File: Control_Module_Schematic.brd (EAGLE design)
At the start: 67 x 47 mm, 30 parts, among them U2 ATMEGA328P_TQFP

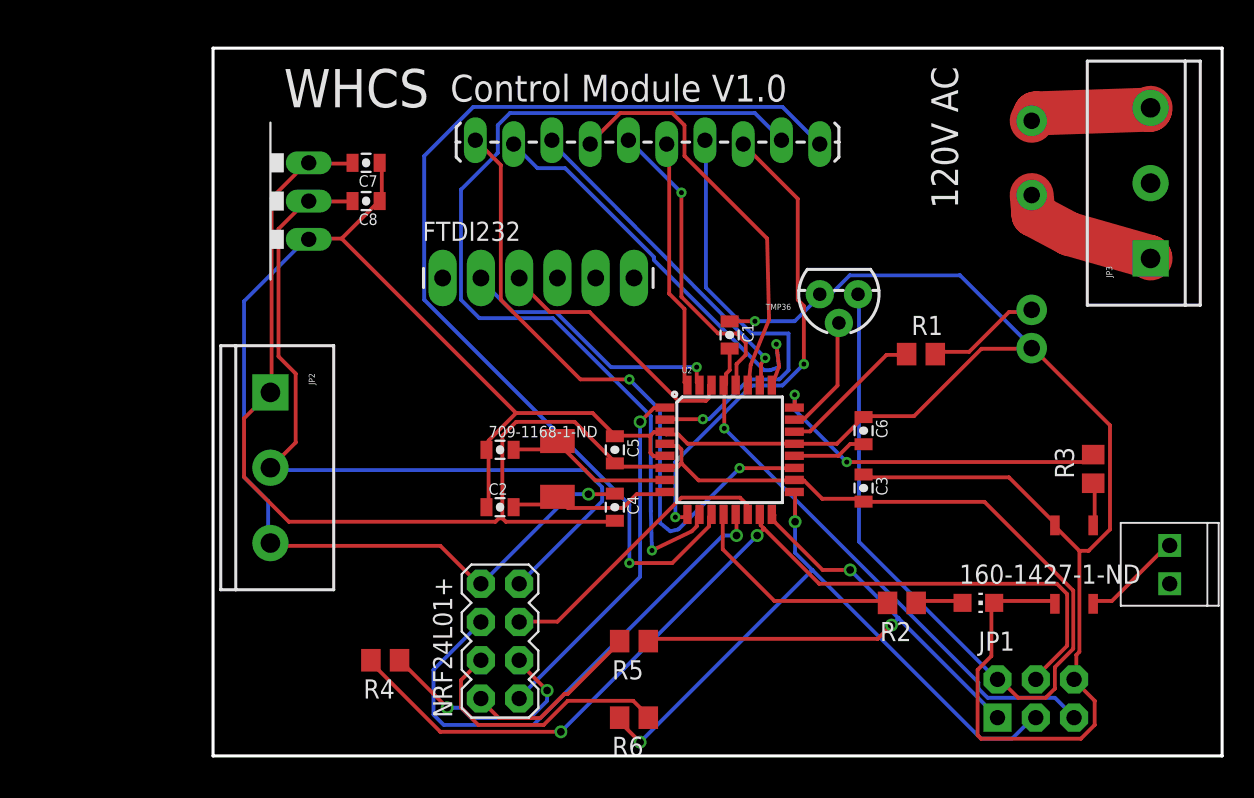
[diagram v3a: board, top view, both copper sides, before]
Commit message: Enhanced crystal footprint
Also did some changing of the route placements to make them have better
spacing.

Added documentation to the TPlace layer to show how the power should be
connected.
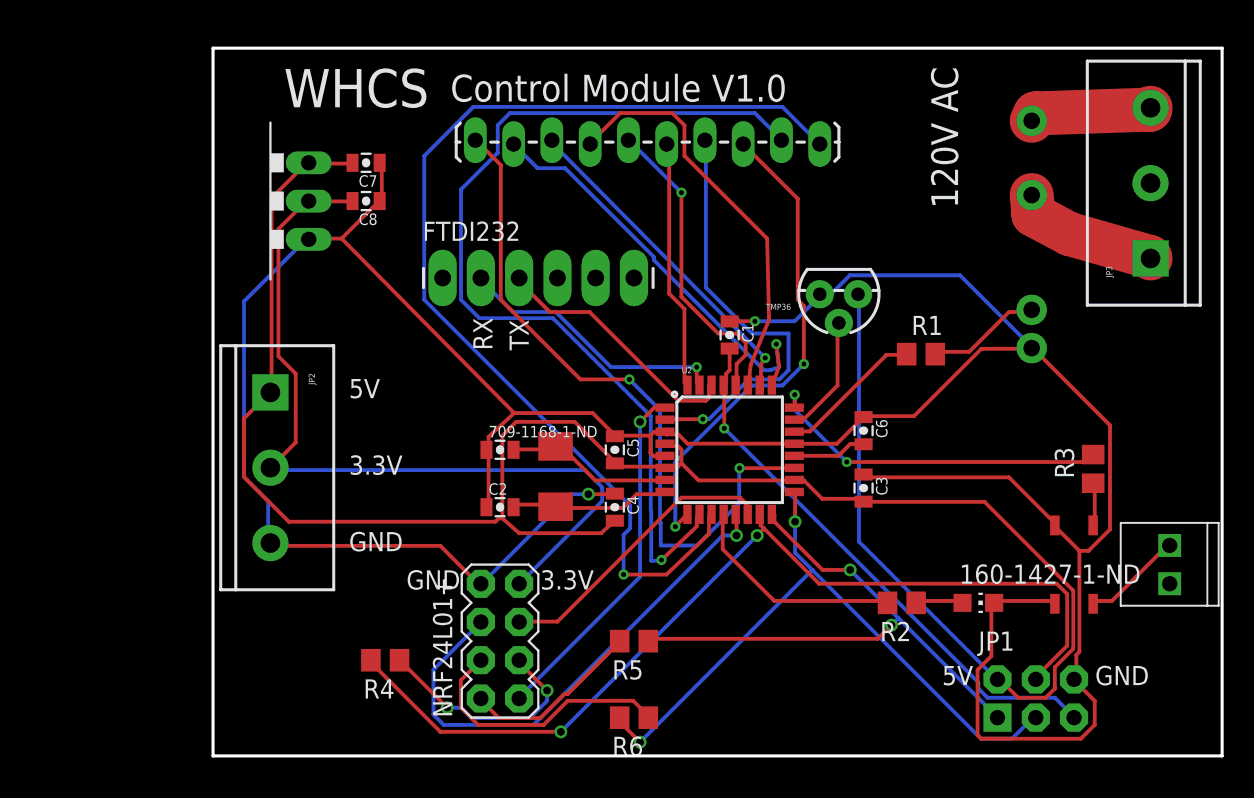
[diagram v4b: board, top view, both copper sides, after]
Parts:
- moved CRYS 0.52 mm to (22.7, 18.5)
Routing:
- net ADC6: track 43.2 -> 46.3 mm
- net PD7: track 68.4 -> 70.4 mm
- net PD6: track 61.5 -> 62.8 mm
- net PD5: track 32.0 -> 32.9 mm
- net 5V: track 143.7 -> 144.3 mm
- net N$15: track 11.1 -> 11.7 mm
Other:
- board text added: "3.3V"
- board text added: "5V"
- board text added: "GND"
- board text added: "RX"
- board text added: "TX"
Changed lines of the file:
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@@
 <text x="15.748" y="43.434" size="1.778" layer="21">Control Module V1.0</text>
 <text x="49.4538" y="36.3347" size="1.778" layer="21" rot="R90">120V AC</text>
+<text x="12.827" y="11.049" size="1.27" layer="21">GND</text>
+<text x="21.717" y="11.049" size="1.27" layer="21">3.3V</text>
+<text x="58.547" y="4.699" size="1.27" layer="21">GND</text>
+<text x="48.387" y="4.699" size="1.27" layer="21">5V</text>
+<text x="17.272" y="29.083" size="1.27" layer="21" rot="R270">RX</text>
+<text x="19.685" y="28.956" size="1.27" layer="21" rot="R270">TX</text>
+<text x="9.017" y="23.749" size="1.27" layer="21">5V</text>
+<text x="9.017" y="13.589" size="1.27" layer="21">GND</text>
+<text x="9.017" y="18.669" size="1.27" layer="21">3.3V</text>
 </plain>
 <attributes>
@@
 <element name="C5" library="SparkFun-Capacitors" package="0805-CAP" value="100nF" x="26.67" y="20.32" rot="R270"/>
 <element name="CPC1002NTR" library="WHCS" package="CPC1002N" value="CPC1002NTR" x="57.15" y="12.7"/>
-<element name="CRYS" library="WHCS" package="CRYS-5X3.2" value="NDK-NX5032GA" x="22.86" y="19.05" rot="R270"/>
+<element name="CRYS" library="WHCS" package="CRYS-5X3.2" value="NDK-NX5032GA" x="22.733" y="18.542" rot="R270"/>
 <element name="FTDI232" library="SparkFun-Connectors" package="1X06_LONGPADS" value="" x="15.24" y="31.7246"/>
 <element name="JP1" library="SparkFun-Connectors" package="2X3-NS" value="AVR_SPI" x="54.61" y="3.81" smashed="yes">
@@
 <wire x1="6.1722" y1="39.3192" x2="6.35" y2="39.37" width="0.254" layer="1"/>
 <wire x1="3.8862" y1="24.2316" x2="3.81" y2="24.13" width="0.254" layer="1"/>
-<wire x1="19.431" y1="15.5448" x2="26.5176" y2="15.5448" width="0.254" layer="1"/>
-<wire x1="19.2024" y1="15.7734" x2="19.431" y2="15.5448" width="0.254" layer="1"/>
+<wire x1="20.32" y1="14.7828" x2="25.7556" y2="14.7828" width="0.254" layer="1"/>
+<wire x1="19.2024" y1="15.7734" x2="20.32" y2="14.7828" width="0.254" layer="1"/>
 <wire x1="19.2024" y1="21.2598" x2="19.2024" y2="15.7734" width="0.254" layer="1"/>
 <wire x1="20.1168" y1="22.1742" x2="19.2024" y2="21.2598" width="0.254" layer="1"/>
 <wire x1="24.003" y1="22.1742" x2="20.1168" y2="22.1742" width="0.254" layer="1"/>
 <wire x1="26.7462" y1="19.431" x2="24.003" y2="22.1742" width="0.254" layer="1"/>
-<wire x1="26.5176" y1="15.5448" x2="26.67" y2="15.61" width="0.254" layer="1"/>
+<wire x1="25.7556" y1="14.7828" x2="26.67" y2="15.61" width="0.254" layer="1"/>
 <wire x1="26.7462" y1="19.431" x2="26.67" y2="19.42" width="0.254" layer="1"/>
 <wire x1="26.7462" y1="19.2024" x2="29.9466" y2="19.2024" width="0.254" layer="1"/>
@@
 <wire x1="10.9728" y1="36.7792" x2="11.06" y2="36.83" width="0.254" layer="1"/>
 <wire x1="6.5024" y1="34.3408" x2="6.35" y2="34.29" width="0.254" layer="1"/>
-<wire x1="18.288" y1="20.9296" x2="18.288" y2="20.32" width="0.254" layer="1"/>
-<wire x1="20.1168" y1="22.7584" x2="18.288" y2="20.9296" width="0.254" layer="1"/>
-<wire x1="25.1968" y1="22.7584" x2="20.1168" y2="22.7584" width="0.254" layer="1"/>
+<wire x1="18.288" y1="21.1836" x2="18.288" y2="20.32" width="0.254" layer="1"/>
+<wire x1="19.9898" y1="22.7584" x2="18.288" y2="21.1836" width="0.254" layer="1"/>
+<wire x1="25.1968" y1="22.7584" x2="19.9898" y2="22.7584" width="0.254" layer="1"/>
 <wire x1="26.6192" y1="21.336" x2="25.1968" y2="22.7584" width="0.254" layer="1"/>
 <wire x1="18.288" y1="20.32" x2="18.15" y2="20.32" width="0.254" layer="1"/>
 <wire x1="26.6192" y1="21.336" x2="26.67" y2="21.22" width="0.254" layer="1"/>
-<wire x1="20.1168" y1="22.7584" x2="8.5344" y2="34.3408" width="0.254" layer="1"/>
+<wire x1="19.9898" y1="22.7584" x2="8.5344" y2="34.3408" width="0.254" layer="1"/>
 <wire x1="31.496" y1="20.7264" x2="38.4048" y2="20.7264" width="0.254" layer="1"/>
 <wire x1="30.8864" y1="21.336" x2="31.496" y2="20.7264" width="0.254" layer="1"/>
@@
 <wire x1="22.86" y1="20.8026" x2="25.3746" y2="18.288" width="0.254" layer="1"/>
 <wire x1="29.9466" y1="18.288" x2="29.9974" y2="18.32" width="0.254" layer="1"/>
-<wire x1="22.86" y1="20.8026" x2="22.86" y2="20.9" width="0.254" layer="1"/>
+<wire x1="22.86" y1="20.8026" x2="22.733" y2="20.542" width="0.254" layer="1"/>
 </signal>
 <signal name="N$15">
@@
 <wire x1="22.86" y1="17.145" x2="23.5458" y2="16.4592" width="0.254" layer="1"/>
 <wire x1="29.9466" y1="17.3736" x2="29.9974" y2="17.52" width="0.254" layer="1"/>
-<wire x1="22.86" y1="17.145" x2="22.86" y2="17.2" width="0.254" layer="1"/>
+<wire x1="22.86" y1="17.145" x2="22.733" y2="16.542" width="0.254" layer="1"/>
 </signal>
 <signal name="N$16">
@@
 <contactref element="JP4" pad="8"/>
 <contactref element="U2" pad="9"/>
-<wire x1="30.6832" y1="15.8496" x2="31.2928" y2="15.8496" width="0.254" layer="1"/>
-<wire x1="30.6832" y1="19.5072" x2="30.6832" y2="15.8496" width="0.254" layer="16"/>
+<wire x1="30.6832" y1="15.2146" x2="31.2928" y2="15.8496" width="0.254" layer="1"/>
+<wire x1="30.6832" y1="19.5072" x2="30.6832" y2="15.2146" width="0.254" layer="16"/>
 <wire x1="35.7632" y1="24.5872" x2="30.6832" y2="19.5072" width="0.254" layer="16"/>
 <wire x1="37.7952" y1="24.5872" x2="35.7632" y2="24.5872" width="0.254" layer="16"/>
@@
 <wire x1="31.2928" y1="15.8496" x2="31.49" y2="16.0274" width="0.254" layer="1"/>
 <wire x1="35.3568" y1="40.4368" x2="35.1917" y2="40.6146" width="0.254" layer="1"/>
-<via x="30.6832" y="15.8496" extent="1-16" drill="0.3302"/>
+<via x="30.6832" y="15.2146" extent="1-16" drill="0.3302"/>
 <via x="39.2176" y="26.0096" extent="1-16" drill="0.3302"/>
 </signal>
@@
 <wire x1="32.1056" y1="15.24" x2="32.1056" y2="15.8496" width="0.254" layer="1"/>
 <wire x1="31.7754" y1="14.9098" x2="32.1056" y2="15.24" width="0.254" layer="1"/>
-<wire x1="29.1338" y1="13.6398" x2="31.7754" y2="14.9098" width="0.254" layer="1"/>
-<wire x1="29.0576" y1="16.256" x2="29.1338" y2="13.6398" width="0.254" layer="16"/>
+<wire x1="31.7754" y1="14.9098" x2="29.7688" y2="13.0048" width="0.254" layer="1"/>
 <wire x1="29.0576" y1="22.5552" x2="29.0576" y2="16.256" width="0.254" layer="16"/>
 <wire x1="22.5552" y1="29.0576" x2="29.0576" y2="22.5552" width="0.254" layer="16"/>
@@
 <wire x1="32.1056" y1="15.8496" x2="32.29" y2="16.0274" width="0.254" layer="1"/>
 <wire x1="37.592" y1="41.0464" x2="37.7317" y2="40.8686" width="0.254" layer="16"/>
-<via x="29.1338" y="13.6398" extent="1-16" drill="0.3302"/>
+<via x="29.7688" y="13.0048" extent="1-16" drill="0.3302"/>
+<wire x1="29.0576" y1="16.256" x2="29.083" y2="16.256" width="0.254" layer="16"/>
+<wire x1="29.083" y1="16.256" x2="29.083" y2="12.954" width="0.254" layer="16"/>
+<wire x1="29.083" y1="12.954" x2="29.7688" y2="12.954" width="0.254" layer="16"/>
+<wire x1="29.7688" y1="12.954" x2="29.7688" y2="13.0048" width="0.254" layer="16"/>
 </signal>
 <signal name="PD7">
 <contactref element="JP4" pad="10"/>
 <contactref element="U2" pad="11"/>
-<wire x1="32.9184" y1="15.24" x2="32.9184" y2="15.8496" width="0.254" layer="1"/>
-<wire x1="30.48" y1="12.8016" x2="32.9184" y2="15.24" width="0.254" layer="1"/>
-<wire x1="27.6352" y1="12.8016" x2="30.48" y2="12.8016" width="0.254" layer="1"/>
-<wire x1="27.6352" y1="16.6624" x2="27.6352" y2="12.8016" width="0.254" layer="16"/>
-<wire x1="14.0208" y1="30.2768" x2="27.6352" y2="16.6624" width="0.254" layer="16"/>
+<wire x1="32.9184" y1="14.732" x2="32.9184" y2="15.8496" width="0.254" layer="1"/>
+<wire x1="30.099" y1="12.0396" x2="32.9184" y2="14.732" width="0.254" layer="1"/>
+<wire x1="27.2542" y1="12.0396" x2="30.099" y2="12.0396" width="0.254" layer="1"/>
+<wire x1="14.0208" y1="30.2768" x2="27.686" y2="16.6116" width="0.254" layer="16"/>
 <wire x1="14.0208" y1="39.8272" x2="14.0208" y2="30.2768" width="0.254" layer="16"/>
 <wire x1="17.272" y1="43.0784" x2="14.0208" y2="39.8272" width="0.254" layer="16"/>
@@
 <wire x1="32.9184" y1="15.8496" x2="33.09" y2="16.0274" width="0.254" layer="1"/>
 <wire x1="40.2336" y1="40.64" x2="40.2717" y2="40.6146" width="0.254" layer="16"/>
-<via x="27.6352" y="12.8016" extent="1-16" drill="0.3302"/>
+<via x="27.2542" y="12.0396" extent="1-16" drill="0.3302"/>
+<wire x1="27.2542" y1="12.0396" x2="27.2542" y2="14.6812" width="0.254" layer="16"/>
+<wire x1="27.2542" y1="14.6812" x2="27.686" y2="15.113" width="0.254" layer="16"/>
+<wire x1="27.686" y1="15.113" x2="27.686" y2="16.6116" width="0.254" layer="16"/>
 </signal>
 <signal name="N$12">
@@
 <contactref element="U2" pad="19"/>
 <wire x1="34.9504" y1="19.1008" x2="38.4048" y2="19.1008" width="0.254" layer="1"/>
-<wire x1="30.8864" y1="15.0368" x2="34.9504" y2="19.1008" width="0.254" layer="16"/>
-<wire x1="30.353" y1="14.9098" x2="30.8864" y2="15.0368" width="0.254" layer="16"/>
-<wire x1="29.6672" y1="15.4686" x2="30.353" y2="14.9098" width="0.254" layer="16"/>
 <wire x1="29.6672" y1="22.9616" x2="29.6672" y2="15.4686" width="0.254" layer="16"/>
 <wire x1="27.6352" y1="24.9936" x2="29.6672" y2="22.9616" width="0.254" layer="16"/>
@@
 <via x="34.9504" y="19.1008" extent="1-16" drill="0.3302"/>
 <via x="27.6352" y="24.9936" extent="1-16" drill="0.3302"/>
+<wire x1="29.6672" y1="15.4686" x2="29.718" y2="15.4686" width="0.254" layer="16"/>
+<wire x1="29.718" y1="15.4686" x2="29.718" y2="13.97" width="0.254" layer="16"/>
+<wire x1="29.718" y1="13.97" x2="32.131" y2="13.97" width="0.254" layer="16"/>
+<wire x1="32.131" y1="13.97" x2="34.925" y2="16.764" width="0.254" layer="16"/>
+<wire x1="34.925" y1="16.764" x2="34.925" y2="19.0754" width="0.254" layer="16"/>
+<wire x1="34.925" y1="19.0754" x2="34.9504" y2="19.1008" width="0.254" layer="16"/>
 </signal>
 </signals>
